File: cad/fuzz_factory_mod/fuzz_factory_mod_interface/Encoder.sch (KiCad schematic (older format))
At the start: 15 parts, among them Q1901 DTA123Y, Q1902 DTA123Y, SW1901 PEL12D-4225S-S2024

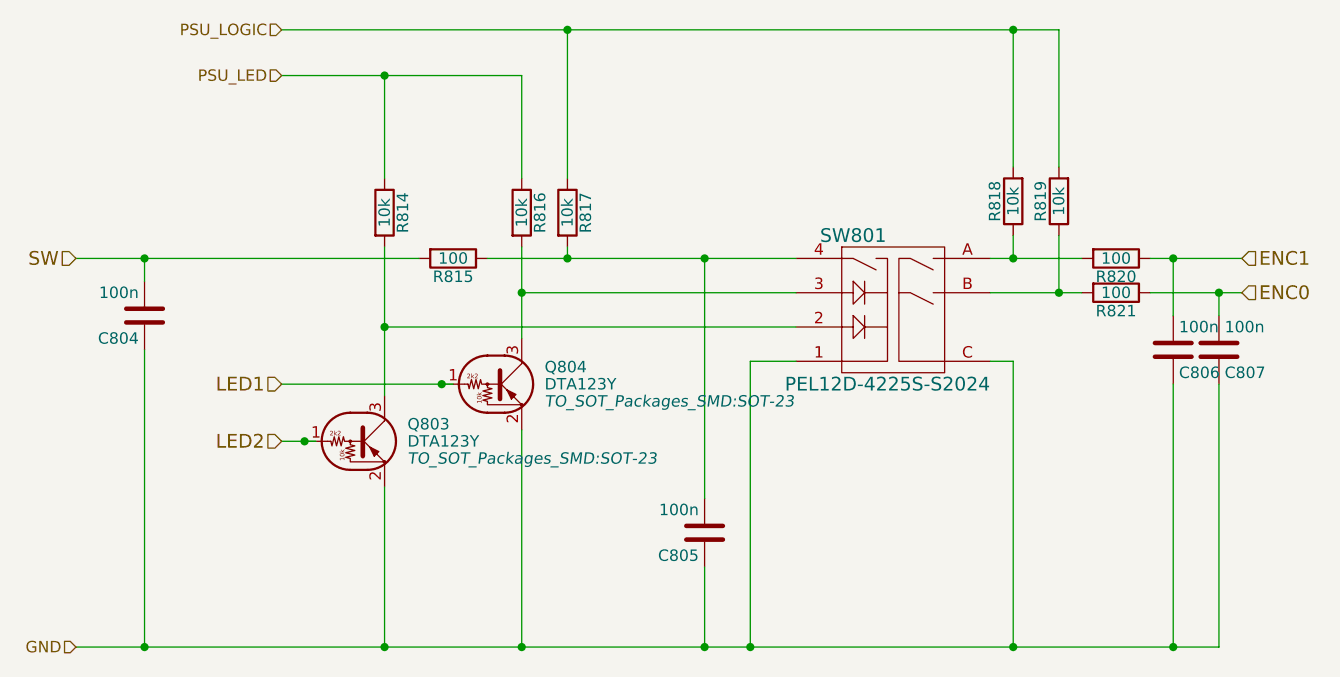
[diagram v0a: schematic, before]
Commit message: Changes architecture.
Corrections on schematic.
Continued Layout placement.
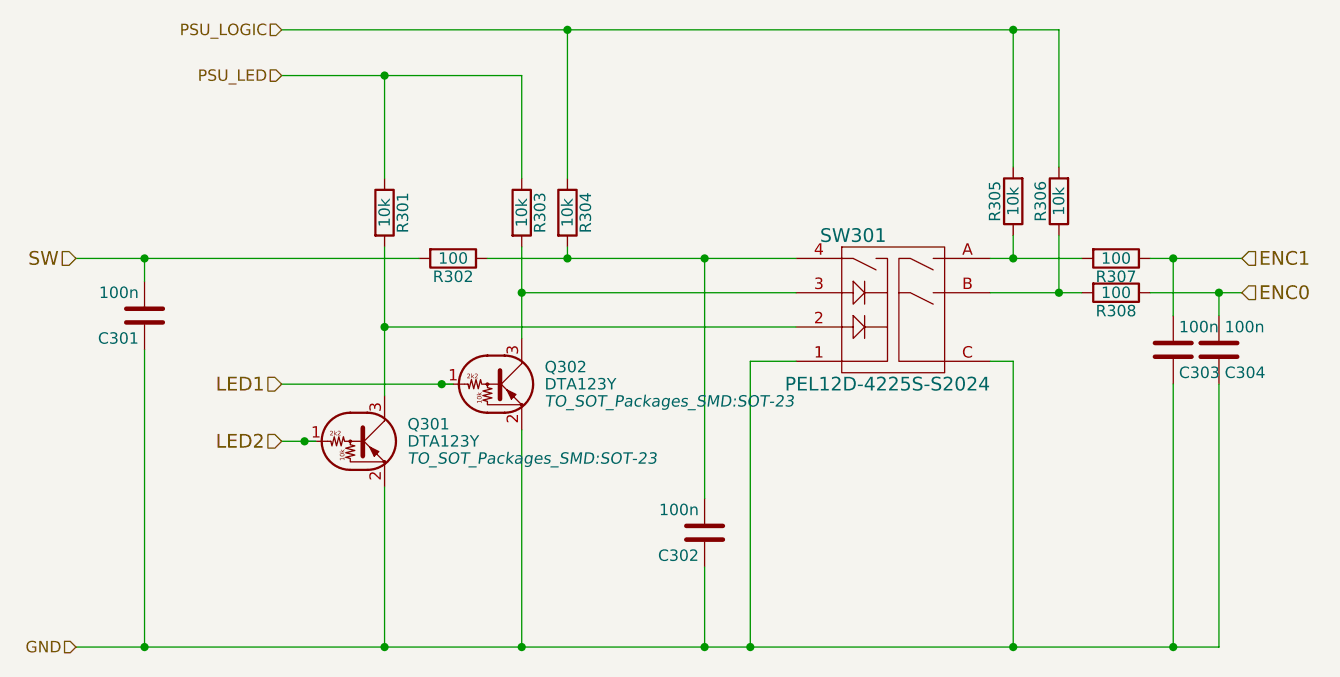
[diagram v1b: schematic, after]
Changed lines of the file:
@@
 EESchema Schematic File Version 4
-LIBS:fuzz_factory_mod-cache
+LIBS:fuzz_factory_mod_interface-cache
 EELAYER 30 0
 EELAYER END
 $Descr A4 11693 8268
 encoding utf-8
-Sheet 8 30
+Sheet 3 5
 Title ""
 Date ""
@@
 AR Path="/5DE4AD26/5EEFDD5E/5E2DCD79/5E256B56" Ref="SW701"  Part="1"
 AR Path="/5DE4AD26/5EEFDD5E/5E2E8544/5E256B56" Ref="SW801"  Part="1"
-F 0 "SW801" H 5900 4300 60  0000 C CNN
+AR Path="/5ED72B13/5E243285/5E256B56" Ref="SW301"  Part="1"
+AR Path="/5ED72B13/5E2DCD79/5E256B56" Ref="SW401"  Part="1"
+AR Path="/5ED72B13/5E2E8544/5E256B56" Ref="SW501"  Part="1"
+F 0 "SW301" H 5900 4300 60  0000 C CNN
 F 1 "PEL12D-4225S-S2024" H 6050 3650 60  0000 C CNN
 F 2 "flax_lib:PEL12D" H 5900 4300 60  0001 C CNN
@@
 AR Path="/5DE4AD26/5EEFDD5E/5E2DCD79/5E256B67" Ref="Q702"  Part="1"
 AR Path="/5DE4AD26/5EEFDD5E/5E2E8544/5E256B67" Ref="Q804"  Part="1"
-F 0 "Q804" H 4550 3925 50  0000 L CNN
+AR Path="/5ED72B13/5E243285/5E256B67" Ref="Q302"  Part="1"
+AR Path="/5ED72B13/5E2DCD79/5E256B67" Ref="Q402"  Part="1"
+AR Path="/5ED72B13/5E2E8544/5E256B67" Ref="Q502"  Part="1"
+F 0 "Q302" H 4550 3925 50  0000 L CNN
 F 1 "DTA123Y" H 4550 3850 50  0000 L CNN
 F 2 "TO_SOT_Packages_SMD:SOT-23" H 4550 3775 50  0000 L CIN
@@
 AR Path="/5DE4AD26/5EEFDD5E/5E2DCD79/5E256B6D" Ref="Q701"  Part="1"
 AR Path="/5DE4AD26/5EEFDD5E/5E2E8544/5E256B6D" Ref="Q803"  Part="1"
-F 0 "Q803" H 3950 4175 50  0000 L CNN
+AR Path="/5ED72B13/5E243285/5E256B6D" Ref="Q301"  Part="1"
+AR Path="/5ED72B13/5E2DCD79/5E256B6D" Ref="Q401"  Part="1"
+AR Path="/5ED72B13/5E2E8544/5E256B6D" Ref="Q501"  Part="1"
+F 0 "Q301" H 3950 4175 50  0000 L CNN
 F 1 "DTA123Y" H 3950 4100 50  0000 L CNN
 F 2 "TO_SOT_Packages_SMD:SOT-23" H 3950 4025 50  0000 L CIN
@@
 AR Path="/5DE4AD26/5EEFDD5E/5E2DCD79/5E256B73" Ref="R704"  Part="1"
 AR Path="/5DE4AD26/5EEFDD5E/5E2E8544/5E256B73" Ref="R817"  Part="1"
-F 0 "R817" V 4730 3100 50  0000 C CNN
+AR Path="/5ED72B13/5E243285/5E256B73" Ref="R304"  Part="1"
+AR Path="/5ED72B13/5E2DCD79/5E256B73" Ref="R404"  Part="1"
+AR Path="/5ED72B13/5E2E8544/5E256B73" Ref="R504"  Part="1"
+F 0 "R304" V 4730 3100 50  0000 C CNN
 F 1 "10k" V 4650 3100 50  0000 C CNN
 F 2 "Resistors_SMD:R_0603" V 4580 3100 50  0001 C CNN
@@
 AR Path="/5DE4AD26/5EEFDD5E/5E2DCD79/5E256B79" Ref="R703"  Part="1"
 AR Path="/5DE4AD26/5EEFDD5E/5E2E8544/5E256B79" Ref="R816"  Part="1"
-F 0 "R816" V 4530 3100 50  0000 C CNN
+AR Path="/5ED72B13/5E243285/5E256B79" Ref="R303"  Part="1"
+AR Path="/5ED72B13/5E2DCD79/5E256B79" Ref="R403"  Part="1"
+AR Path="/5ED72B13/5E2E8544/5E256B79" Ref="R503"  Part="1"
+F 0 "R303" V 4530 3100 50  0000 C CNN
 F 1 "10k" V 4450 3100 50  0000 C CNN
 F 2 "Resistors_SMD:R_0603" V 4380 3100 50  0001 C CNN
@@
 AR Path="/5DE4AD26/5EEFDD5E/5E2DCD79/5E256B7F" Ref="R701"  Part="1"
 AR Path="/5DE4AD26/5EEFDD5E/5E2E8544/5E256B7F" Ref="R814"  Part="1"
-F 0 "R814" V 3930 3100 50  0000 C CNN
+AR Path="/5ED72B13/5E243285/5E256B7F" Ref="R301"  Part="1"
+AR Path="/5ED72B13/5E2DCD79/5E256B7F" Ref="R401"  Part="1"
+AR Path="/5ED72B13/5E2E8544/5E256B7F" Ref="R501"  Part="1"
+F 0 "R301" V 3930 3100 50  0000 C CNN
 F 1 "10k" V 3850 3100 50  0000 C CNN
 F 2 "Resistors_SMD:R_0603" V 3780 3100 50  0001 C CNN
@@
 AR Path="/5DE4AD26/5EEFDD5E/5E2DCD79/5E256BA3" Ref="C704"  Part="1"
 AR Path="/5DE4AD26/5EEFDD5E/5E2E8544/5E256BA3" Ref="C805"  Part="1"
-F 0 "C805" H 5275 4600 50  0000 L CNN
+AR Path="/5ED72B13/5E243285/5E256BA3" Ref="C302"  Part="1"
+AR Path="/5ED72B13/5E2DCD79/5E256BA3" Ref="C402"  Part="1"
+AR Path="/5ED72B13/5E2E8544/5E256BA3" Ref="C502"  Part="1"
+F 0 "C302" H 5275 4600 50  0000 L CNN
 F 1 "100n" H 5275 4400 50  0000 L CNN
 F 2 "Capacitors_SMD:C_0603" H 5288 4350 50  0001 C CNN
@@
 AR Path="/5DE4AD26/5EEFDD5E/5E2DCD79/5E256BAF" Ref="R707"  Part="1"
 AR Path="/5DE4AD26/5EEFDD5E/5E2E8544/5E256BAF" Ref="R820"  Part="1"
-F 0 "R820" V 7130 3300 50  0000 C CNN
+AR Path="/5ED72B13/5E243285/5E256BAF" Ref="R307"  Part="1"
+AR Path="/5ED72B13/5E2DCD79/5E256BAF" Ref="R407"  Part="1"
+AR Path="/5ED72B13/5E2E8544/5E256BAF" Ref="R507"  Part="1"
+F 0 "R307" V 7130 3300 50  0000 C CNN
 F 1 "100" V 7050 3300 50  0000 C CNN
 F 2 "Resistors_SMD:R_0603" V 6980 3300 50  0001 C CNN
@@
 AR Path="/5DE4AD26/5EEFDD5E/5E2DCD79/5E256BB5" Ref="R708"  Part="1"
 AR Path="/5DE4AD26/5EEFDD5E/5E2E8544/5E256BB5" Ref="R821"  Part="1"
-F 0 "R821" V 7130 3450 50  0000 C CNN
+AR Path="/5ED72B13/5E243285/5E256BB5" Ref="R308"  Part="1"
+AR Path="/5ED72B13/5E2DCD79/5E256BB5" Ref="R408"  Part="1"
+AR Path="/5ED72B13/5E2E8544/5E256BB5" Ref="R508"  Part="1"
+F 0 "R308" V 7130 3450 50  0000 C CNN
 F 1 "100" V 7050 3450 50  0000 C CNN
 F 2 "Resistors_SMD:R_0603" V 6980 3450 50  0001 C CNN
@@
 AR Path="/5DE4AD26/5EEFDD5E/5E2DCD79/5E256BBB" Ref="C705"  Part="1"
 AR Path="/5DE4AD26/5EEFDD5E/5E2E8544/5E256BBB" Ref="C806"  Part="1"
-F 0 "C806" H 7325 3800 50  0000 L CNN
+AR Path="/5ED72B13/5E243285/5E256BBB" Ref="C303"  Part="1"
+AR Path="/5ED72B13/5E2DCD79/5E256BBB" Ref="C403"  Part="1"
+AR Path="/5ED72B13/5E2E8544/5E256BBB" Ref="C503"  Part="1"
+F 0 "C303" H 7325 3800 50  0000 L CNN
 F 1 "100n" H 7325 3600 50  0000 L CNN
 F 2 "Capacitors_SMD:C_0603" H 7338 3550 50  0001 C CNN
@@
 AR Path="/5DE4AD26/5EEFDD5E/5E2DCD79/5E256BC1" Ref="C706"  Part="1"
 AR Path="/5DE4AD26/5EEFDD5E/5E2E8544/5E256BC1" Ref="C807"  Part="1"
-F 0 "C807" H 7525 3800 50  0000 L CNN
+AR Path="/5ED72B13/5E243285/5E256BC1" Ref="C304"  Part="1"
+AR Path="/5ED72B13/5E2DCD79/5E256BC1" Ref="C404"  Part="1"
+AR Path="/5ED72B13/5E2E8544/5E256BC1" Ref="C504"  Part="1"
+F 0 "C304" H 7525 3800 50  0000 L CNN
 F 1 "100n" H 7525 3600 50  0000 L CNN
 F 2 "Capacitors_SMD:C_0603" H 7538 3550 50  0001 C CNN
@@
 AR Path="/5DE4AD26/5EEFDD5E/5E2DCD79/5E256BD9" Ref="R705"  Part="1"
 AR Path="/5DE4AD26/5EEFDD5E/5E2E8544/5E256BD9" Ref="R818"  Part="1"
-F 0 "R818" V 6680 3050 50  0000 C CNN
+AR Path="/5ED72B13/5E243285/5E256BD9" Ref="R305"  Part="1"
+AR Path="/5ED72B13/5E2DCD79/5E256BD9" Ref="R405"  Part="1"
+AR Path="/5ED72B13/5E2E8544/5E256BD9" Ref="R505"  Part="1"
+F 0 "R305" V 6680 3050 50  0000 C CNN
 F 1 "10k" V 6600 3050 50  0000 C CNN
 F 2 "Resistors_SMD:R_0603" V 6530 3050 50  0001 C CNN
@@
 AR Path="/5DE4AD26/5EEFDD5E/5E2DCD79/5E256BDF" Ref="R706"  Part="1"
 AR Path="/5DE4AD26/5EEFDD5E/5E2E8544/5E256BDF" Ref="R819"  Part="1"
-F 0 "R819" V 6880 3050 50  0000 C CNN
+AR Path="/5ED72B13/5E243285/5E256BDF" Ref="R306"  Part="1"
+AR Path="/5ED72B13/5E2DCD79/5E256BDF" Ref="R406"  Part="1"
+AR Path="/5ED72B13/5E2E8544/5E256BDF" Ref="R506"  Part="1"
+F 0 "R306" V 6880 3050 50  0000 C CNN
 F 1 "10k" V 6800 3050 50  0000 C CNN
 F 2 "Resistors_SMD:R_0603" V 6730 3050 50  0001 C CNN
@@
 AR Path="/5DE4AD26/5EEFDD5E/5E2DCD79/5E256BF1" Ref="R702"  Part="1"
 AR Path="/5DE4AD26/5EEFDD5E/5E2E8544/5E256BF1" Ref="R815"  Part="1"
-F 0 "R815" V 4230 3300 50  0000 C CNN
+AR Path="/5ED72B13/5E243285/5E256BF1" Ref="R302"  Part="1"
+AR Path="/5ED72B13/5E2DCD79/5E256BF1" Ref="R402"  Part="1"
+AR Path="/5ED72B13/5E2E8544/5E256BF1" Ref="R502"  Part="1"
+F 0 "R302" V 4230 3300 50  0000 C CNN
 F 1 "100" V 4150 3300 50  0000 C CNN
 F 2 "Resistors_SMD:R_0603" V 4080 3300 50  0001 C CNN
@@
 AR Path="/5DE4AD26/5EEFDD5E/5E2DCD79/5E256BF7" Ref="C703"  Part="1"
 AR Path="/5DE4AD26/5EEFDD5E/5E2E8544/5E256BF7" Ref="C804"  Part="1"
-F 0 "C804" H 2825 3650 50  0000 L CNN
+AR Path="/5ED72B13/5E243285/5E256BF7" Ref="C301"  Part="1"
+AR Path="/5ED72B13/5E2DCD79/5E256BF7" Ref="C401"  Part="1"
+AR Path="/5ED72B13/5E2E8544/5E256BF7" Ref="C501"  Part="1"
+F 0 "C301" H 2825 3650 50  0000 L CNN
 F 1 "100n" H 2825 3450 50  0000 L CNN
 F 2 "Capacitors_SMD:C_0603" H 2838 3400 50  0001 C CNN
